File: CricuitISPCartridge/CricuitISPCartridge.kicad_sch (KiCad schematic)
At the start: 3 parts, among them J1 Conn_02x10_Odd_Even, J2 Conn_01x03_Male, J3 AVR-ISP-6

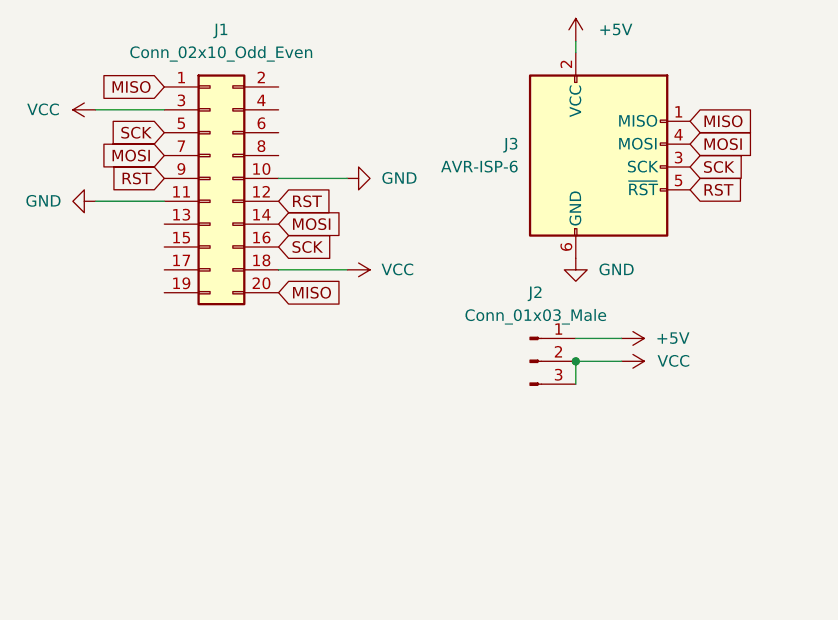
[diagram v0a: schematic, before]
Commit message: Might as well break out all the ports for the cartridge slot.
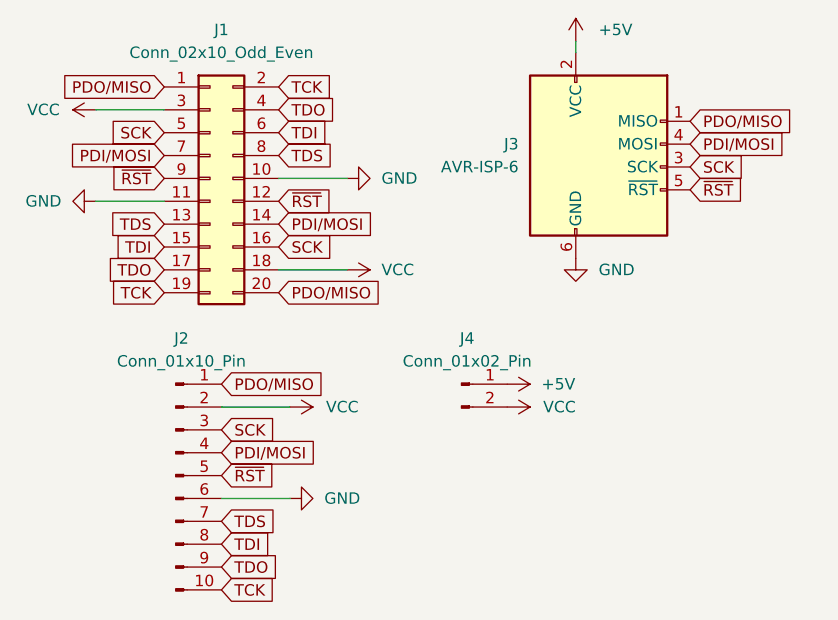
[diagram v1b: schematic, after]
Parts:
- removed J2: Conn_01x03_Male, Connector_PinHeader_2.54mm:PinHeader_1x03_P2.54mm_Vertical, symbol Connector:Conn_01x03_Male
- added J2: Conn_01x10_Pin, Connector_PinHeader_2.54mm:PinHeader_1x10_P2.54mm_Vertical, symbol Connector:Conn_01x10_Pin
- added J4: Conn_01x02_Pin, Connector_PinHeader_2.54mm:PinHeader_1x02_P2.54mm_Vertical, symbol Connector:Conn_01x02_Pin
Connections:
- net +5V: now also J4.1 (Pin_1)
- net GND: now also J2.6 (Pin_6)
- net SCK: now also J2.3 (Pin_3)
- net VCC: now also J2.2 (Pin_2), J4.2 (Pin_2)
- net TDS: now reaches J1.13 (Pin_13)
- net TDS: now also J1.8 (Pin_8), J2.7 (Pin_7)
- net TDI: now reaches J1.15 (Pin_15)
- net TDI: now also J1.6 (Pin_6), J2.8 (Pin_8)
- net TDO: now reaches J1.17 (Pin_17)
- net TDO: now also J1.4 (Pin_4), J2.9 (Pin_9)
- net TCK: now reaches J1.19 (Pin_19)
- net TCK: now also J1.2 (Pin_2), J2.10 (Pin_10)
- net MISO renamed PDO/MISO
- net PDO/MISO: now also J2.1 (Pin_1)
- net MOSI renamed PDI/MOSI
- net PDI/MOSI: now also J2.4 (Pin_4)
- net RST renamed ~{RST}
- net ~{RST}: now also J2.5 (Pin_5)
